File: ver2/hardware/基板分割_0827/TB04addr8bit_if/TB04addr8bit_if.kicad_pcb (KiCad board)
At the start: 2 copper layers, 110 x 135 mm, 110 parts, among them J1 Conn_02x20_Odd_Even, J10 Conn_02x05_Odd_Even, J1001 Conn_01x06_Socket, J1002 Conn_01x06_Socket, J1003 Conn_01x06_Socket, J1004 Conn_01x06_Socket, J101 USB_C_Receptacle_PowerOnly_6P, J11 Conn_02x05_Odd_Even, J12 Conn_02x05_Odd_Even, J13 Conn_02x05_Odd_Even, J1602 Screw_Terminal_01x02, J901 Conn_02x05_Odd_Even, J902 Conn_02x05_Odd_Even, J903 Conn_02x05_Odd_Even, J904 Conn_02x05_Odd_Even, SW1001 SW_DIP_x04, SW1002 SW_DIP_x04, SW1003 SW_DIP_x04, SW1004 SW_DIP_x04, SW101 SW_SPDT, SW501 SW_Push, SW502 sw rotary, SW503 SW_Push, U1001 74HC244, U1002 74HC244, U1003 74HC244, U1004 74HC244, U501 74HC14, U502 4060, U901 74HC377, U902 74HC377, U903 74HC377, U905 74HC377, Y501 32.768KHz

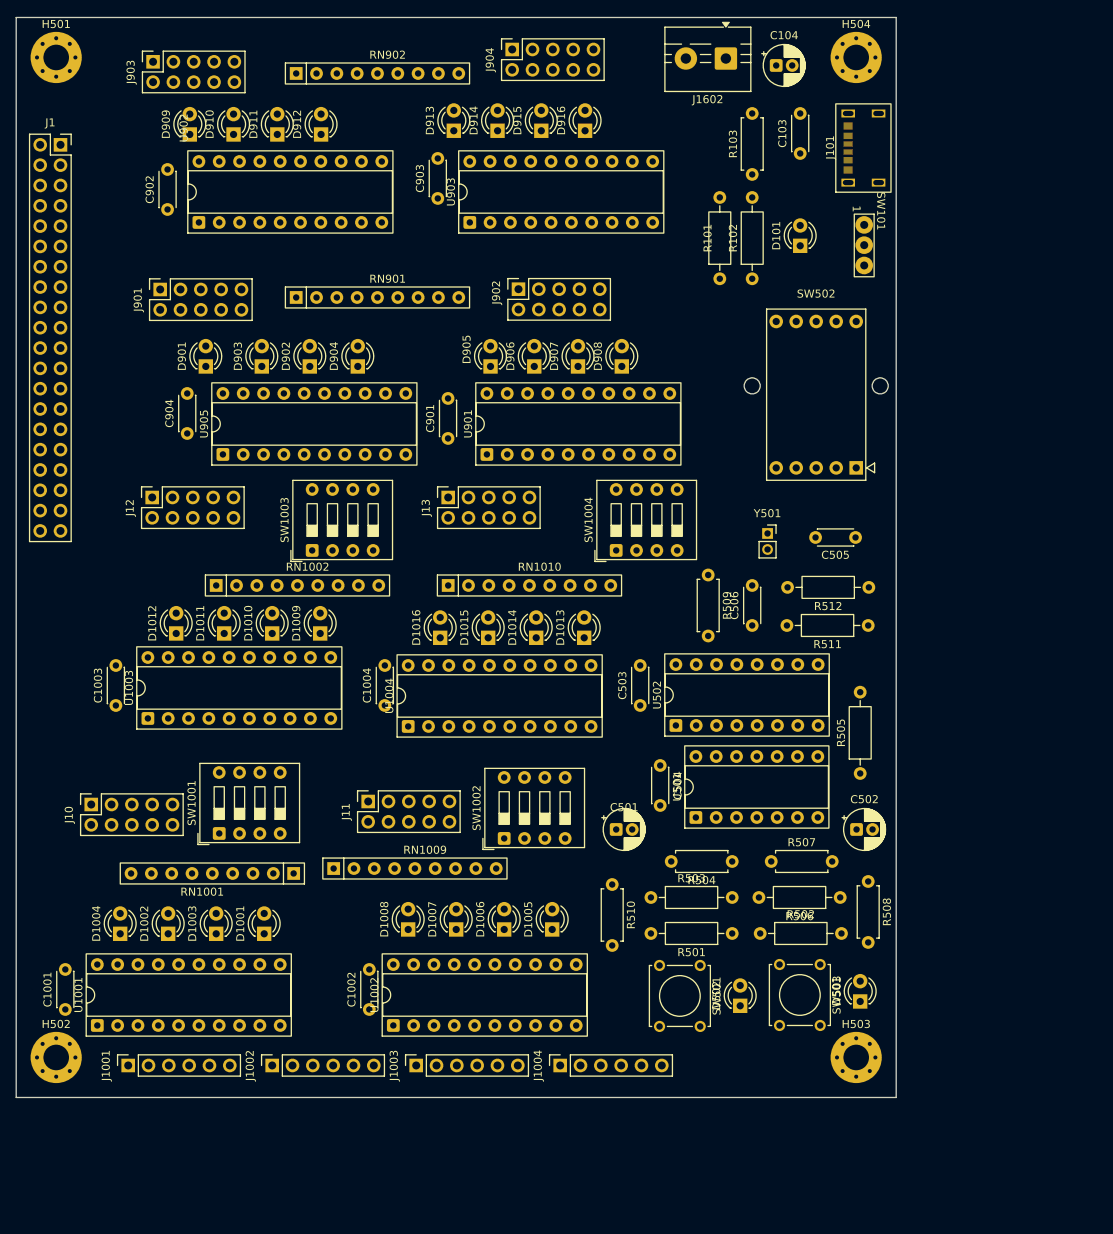
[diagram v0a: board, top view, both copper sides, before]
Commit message: ver2: 3枚の外形を高さ150mmに統一／制御板のプルダウンをSIP集約・取付穴2個追加(配置は途中)
- 外形: 演算130x150・制御200x150・IF135x150
- 制御板: R603-R606(10K x4)をRN602(R_Array_SIP5)へ集約／取付穴H105・H106を追加／U1101のフットプリントをDIP-24_W15.24mm_Socketへ
- 検証: 署名変化は制御8ピン(ネット名のみ・構成員同一)と演算32ピン(同値素子の割り当て替え)だけ／未接続入力0・単一構成員ネット0・回路図とPCBの参照番号差分0
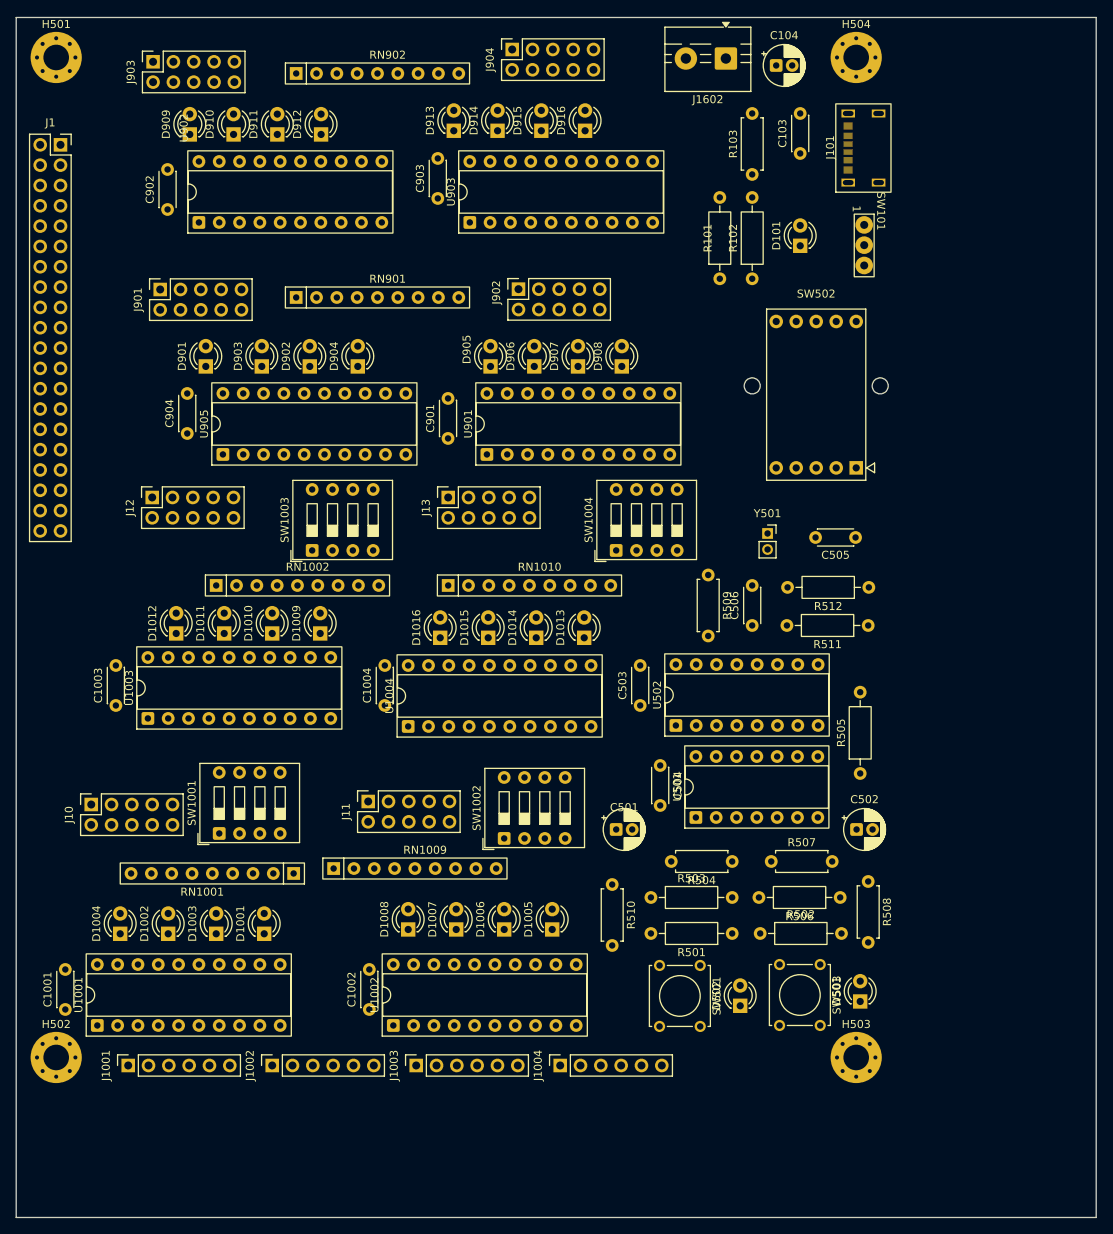
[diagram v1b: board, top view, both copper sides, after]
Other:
- board size 110 x 135 mm -> 135 x 150 mm
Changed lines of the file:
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@@
 	(gr_rect
 		(start 100 50)
-		(end 210 185)
+		(end 235 200)
 		(stroke
 			(width 0.05)
-			(type default)
+			(type solid)
 		)
 		(fill no)

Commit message: ver2: 制御板とIF板の部品配置を更新(ユーザー作業・配線前の復帰点)
- 制御板: 7segIFコネクタ(J6-J9/J801-804)・ZIFソケットU604・SW601・電源(J1602/C104/D101/R103)を演算板と重ならない右側(x240以降)へ／LED7個(D603-606,D1201-1203)を手前側へ
- IF板: 配置を更新
- 実測: 3枚ともパッドの外形外0・courtyard重なり0・配線0(配置段階)。制御板103部品・IF板110部品
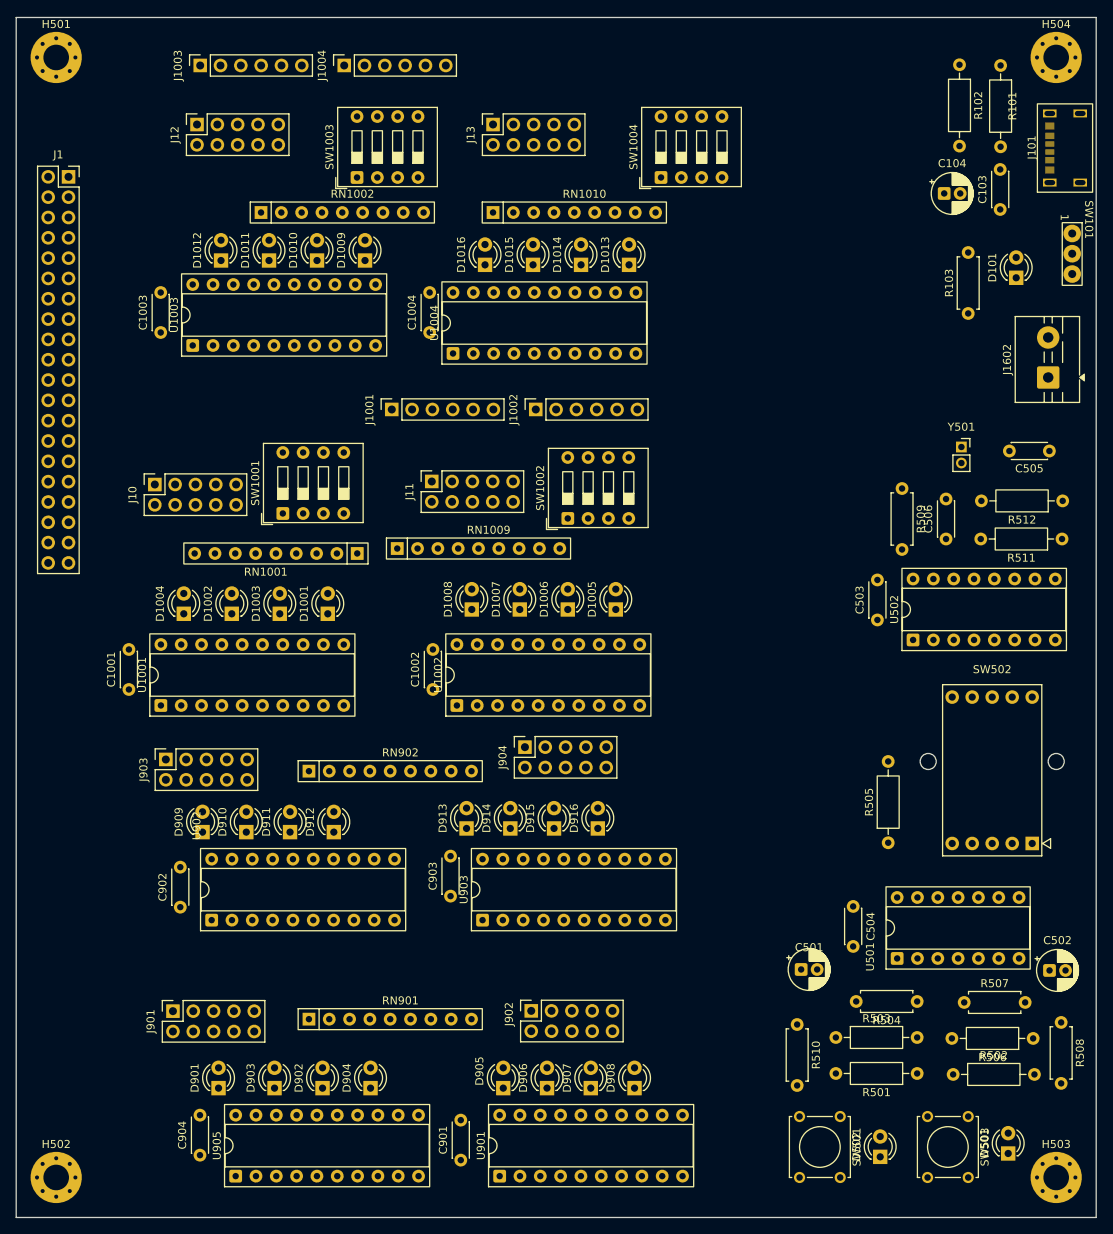
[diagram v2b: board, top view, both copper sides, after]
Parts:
- moved J1003 127.9 mm to (123.0, 56.0)
- moved J1004 127.9 mm to (141.0, 56.0)
- moved C904 90.2 mm to (123.0, 192.2)
- moved J901 90.2 mm to (119.6, 174.2)
- moved RN901 90.2 mm to (136.6, 175.2)
- moved J902 90.2 mm to (164.4, 174.2)
- moved C901 90.2 mm to (155.6, 192.8)
- moved D901 90.2 mm to (125.3, 183.8)
- moved D902 90.2 mm to (138.3, 183.8)
- moved D903 90.2 mm to (132.3, 183.8)
- moved D904 90.2 mm to (144.3, 183.8)
- moved D905 90.2 mm to (160.9, 183.8)
- moved D906 90.2 mm to (166.4, 183.8)
- moved D907 90.2 mm to (171.8, 183.8)
- moved D908 90.2 mm to (177.3, 183.8)
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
